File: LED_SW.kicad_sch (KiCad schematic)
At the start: 32 parts

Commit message: OLED, Relay and Bar graph added
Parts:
- renumbered D to D10, D to D11, D to D12, D to D13, D to D14, D to D15, D to D16, D to D9, R to R12, R to R13, R to R14, R to R15, R to R16, R to R17, R to R18, R to R19, S to S2, S to S3, S to S4, S to S5, S to S6, S to S7, S to S8, S to S9

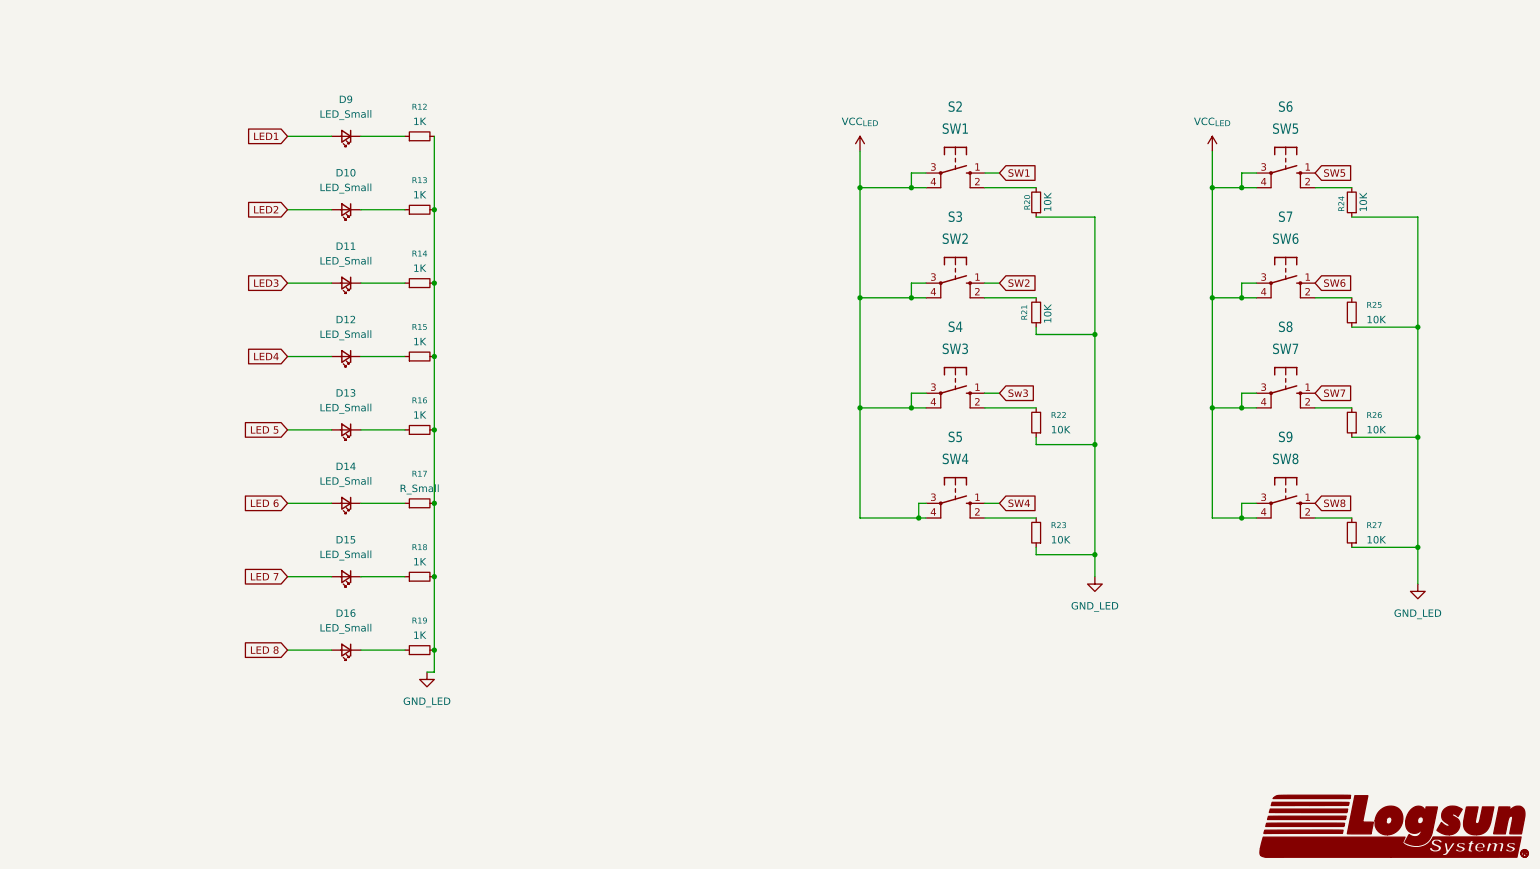
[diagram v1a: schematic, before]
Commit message: Connectors Added
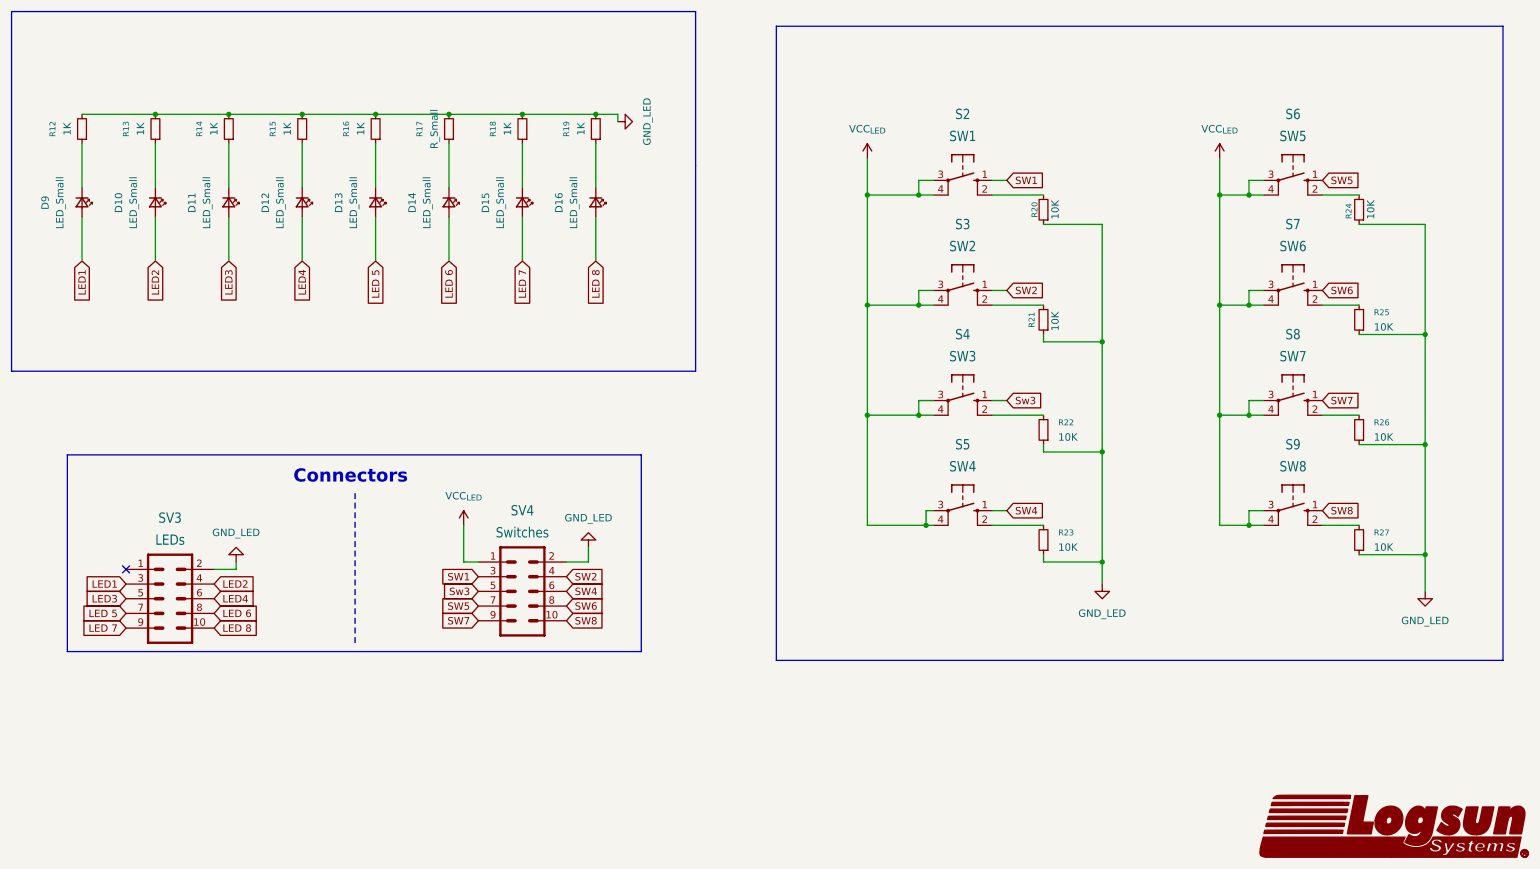
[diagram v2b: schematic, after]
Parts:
- added SV3: LEDs, LOGSUN:LGS-KC-ML10_INTERFACE, symbol LOGSUN:LGS-KC-ML10_INTERFACE
- added SV4: Switches, LOGSUN:LGS-KC-ML10_INTERFACE, symbol LOGSUN:LGS-KC-ML10_INTERFACE
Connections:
- net GND_LED: now also SV3.2, SV4.2
- net LED 5: now also SV3.7
- net LED 6: now also SV3.8
- net LED 7: now also SV3.9
- net LED 8: now also SV3.10
- net LED1: now also SV3.3
- net LED2: now also SV3.4
- net LED3: now also SV3.5
- net LED4: now also SV3.6
- net SW1: now also SV4.3
- net SW2: now also SV4.4
- net SW4: now also SV4.6
- net SW5: now also SV4.7
- net SW6: now also SV4.8
- net SW7: now also SV4.9
- net SW8: now also SV4.10
- net Sw3: now also SV4.5
- net VCC_{LED}: now also SV4.1
- no-connect marks 0 -> 1
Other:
- note added: "Connectors"
- moved on the sheet: D10, D11, D12, D13, D14, D15, D16, D9, R12, R13, R14, R15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

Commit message: Schematic Completed, Footprints Assigned
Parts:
- D10, D11, D12, D13, D14, D15, D16, D9: footprint (none) -> LED_SMD:LED_1206_3216Metric_ReverseMount_Hole1.8x2.4mm
- R12, R13, R14, R15, R16, R18, R19, R20, R21, R22, R23, R24, R25, R26, R27: footprint (none) -> Resistor_SMD:R_0805_2012Metric_Pad1.20x1.40mm_HandSolder
- R17: value R_Small -> 1K; footprint (none) -> Resistor_SMD:R_0805_2012Metric_Pad1.20x1.40mm_HandSolder
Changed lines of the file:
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@@
 			)
 		)
-		(property "Footprint" ""
+		(property "Footprint" "Resistor_SMD:R_0805_2012Metric_Pad1.20x1.40mm_HandSolder"
 			(at 105.41 53.34 0)
 			(effects
@@
 			)
 		)
-		(property "Footprint" ""
+		(property "Footprint" "LED_SMD:LED_1206_3216Metric_ReverseMount_Hole1.8x2.4mm"
 			(at 54.61 66.04 90)
 			(effects
@@
 			)
 		)
-		(property "Footprint" ""
+		(property "Footprint" "Resistor_SMD:R_0805_2012Metric_Pad1.20x1.40mm_HandSolder"
 			(at 80.01 53.34 0)
 			(effects
@@
 			)
 		)
-		(property "Footprint" ""
+		(property "Footprint" "Resistor_SMD:R_0805_2012Metric_Pad1.20x1.40mm_HandSolder"
 			(at 195.58 67.31 0)
 			(effects
@@
 		(fields_autoplaced yes)
 		(property "Reference" "R17"
-			(at 87.63 53.34 90)
+			(at 95.25 52.0699 0)
 			(effects
 				(font
 					(size 1.016 1.016)
 				)
-			)
-		)
-		(property "Value" "R_Small"
-			(at 90.17 53.34 90)
-			(effects
-				(font
-					(size 1.27 1.27)
-				)
-			)
-		)
-		(property "Footprint" ""
+				(justify right)
+			)
+		)
+		(property "Value" "1K"
+			(at 95.25 54.6099 0)
+			(effects
+				(font
+					(size 1.27 1.27)
+				)
+				(justify right)
+			)
+		)
+		(property "Footprint" "Resistor_SMD:R_0805_2012Metric_Pad1.20x1.40mm_HandSolder"
 			(at 92.71 53.34 0)
 			(effects
@@
 			)
 		)
-		(property "Footprint" ""
+		(property "Footprint" "LED_SMD:LED_1206_3216Metric_ReverseMount_Hole1.8x2.4mm"
 			(at 29.21 66.04 90)
 			(effects
@@
 			)
 		)
-		(property "Footprint" ""
+		(property "Footprint" "LED_SMD:LED_1206_3216Metric_ReverseMount_Hole1.8x2.4mm"
 			(at 92.71 66.04 90)
 			(effects
@@
 			)
 		)
-		(property "Footprint" ""
+		(property "Footprint" "Resistor_SMD:R_0805_2012Metric_Pad1.20x1.40mm_HandSolder"
 			(at 250.19 67.31 0)
 			(effects
@@
 			)
 		)
-		(property "Footprint" ""
+		(property "Footprint" "LED_SMD:LED_1206_3216Metric_ReverseMount_Hole1.8x2.4mm"
 			(at 118.11 66.04 90)
 			(effects
@@
 			)
 		)
-		(property "Footprint" ""
+		(property "Footprint" "Resistor_SMD:R_0805_2012Metric_Pad1.20x1.40mm_HandSolder"
 			(at 250.19 124.46 0)
 			(effects
@@
 			)
 		)
-		(property "Footprint" ""
+		(property "Footprint" "Resistor_SMD:R_0805_2012Metric_Pad1.20x1.40mm_HandSolder"
 			(at 41.91 53.34 0)
 			(effects
@@
 			)
 		)
-		(property "Footprint" ""
+		(property "Footprint" "LED_SMD:LED_1206_3216Metric_ReverseMount_Hole1.8x2.4mm"
 			(at 80.01 66.04 90)
 			(effects
@@
 			)
 		)
-		(property "Footprint" ""
+		(property "Footprint" "Resistor_SMD:R_0805_2012Metric_Pad1.20x1.40mm_HandSolder"
 			(at 29.21 53.34 0)
 			(effects
@@
 			)
 		)
-		(property "Footprint" ""
+		(property "Footprint" "Resistor_SMD:R_0805_2012Metric_Pad1.20x1.40mm_HandSolder"
 			(at 118.11 53.34 0)
 			(effects
@@
 			)
 		)
-		(property "Footprint" ""
+		(property "Footprint" "LED_SMD:LED_1206_3216Metric_ReverseMount_Hole1.8x2.4mm"
 			(at 67.31 66.04 90)
 			(effects
@@
 			)
 		)
-		(property "Footprint" ""
+		(property "Footprint" "Resistor_SMD:R_0805_2012Metric_Pad1.20x1.40mm_HandSolder"
 			(at 250.19 86.36 0)
 			(effects
@@
 			)
 		)
-		(property "Footprint" ""
+		(property "Footprint" "LED_SMD:LED_1206_3216Metric_ReverseMount_Hole1.8x2.4mm"
 			(at 105.41 66.04 90)
 			(effects
@@
 			)
 		)
-		(property "Footprint" ""
+		(property "Footprint" "LED_SMD:LED_1206_3216Metric_ReverseMount_Hole1.8x2.4mm"
 			(at 41.91 66.04 90)
 			(effects
@@
 			)
 		)
-		(property "Footprint" ""
+		(property "Footprint" "Resistor_SMD:R_0805_2012Metric_Pad1.20x1.40mm_HandSolder"
 			(at 54.61 53.34 0)
 			(effects
@@
 			)
 		)
-		(property "Footprint" ""
+		(property "Footprint" "Resistor_SMD:R_0805_2012Metric_Pad1.20x1.40mm_HandSolder"
 			(at 195.58 105.41 0)
 			(effects
@@
 			)
 		)
-		(property "Footprint" ""
+		(property "Footprint" "Resistor_SMD:R_0805_2012Metric_Pad1.20x1.40mm_HandSolder"
 			(at 250.19 105.41 0)
 			(effects
@@
 			)
 		)
-		(property "Footprint" ""
+		(property "Footprint" "Resistor_SMD:R_0805_2012Metric_Pad1.20x1.40mm_HandSolder"
 			(at 67.31 53.34 0)
 			(effects
@@
 			)
 		)
-		(property "Footprint" ""
+		(property "Footprint" "Resistor_SMD:R_0805_2012Metric_Pad1.20x1.40mm_HandSolder"
 			(at 195.58 124.46 0)
 			(effects
@@
 			)
 		)
-		(property "Footprint" ""
+		(property "Footprint" "Resistor_SMD:R_0805_2012Metric_Pad1.20x1.40mm_HandSolder"
 			(at 195.58 86.36 0)
 			(effects

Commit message: Bar LED Resistors Added & Mounting holes added
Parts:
- D10, D11, D12, D13, D14, D15, D16, D9: footprint LED_SMD:LED_1206_3216Metric_ReverseMount_Hole1.8x2.4mm -> LED_SMD:LED_1206_3216Metric_Pad1.42x1.75mm_HandSolder
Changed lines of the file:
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@@
 			)
 		)
-		(property "Footprint" "LED_SMD:LED_1206_3216Metric_ReverseMount_Hole1.8x2.4mm"
+		(property "Footprint" "LED_SMD:LED_1206_3216Metric_Pad1.42x1.75mm_HandSolder"
 			(at 54.61 66.04 90)
 			(effects
@@
 			)
 		)
-		(property "Footprint" "LED_SMD:LED_1206_3216Metric_ReverseMount_Hole1.8x2.4mm"
+		(property "Footprint" "LED_SMD:LED_1206_3216Metric_Pad1.42x1.75mm_HandSolder"
 			(at 29.21 66.04 90)
 			(effects
@@
 			)
 		)
-		(property "Footprint" "LED_SMD:LED_1206_3216Metric_ReverseMount_Hole1.8x2.4mm"
+		(property "Footprint" "LED_SMD:LED_1206_3216Metric_Pad1.42x1.75mm_HandSolder"
 			(at 92.71 66.04 90)
 			(effects
@@
 			)
 		)
-		(property "Footprint" "LED_SMD:LED_1206_3216Metric_ReverseMount_Hole1.8x2.4mm"
+		(property "Footprint" "LED_SMD:LED_1206_3216Metric_Pad1.42x1.75mm_HandSolder"
 			(at 118.11 66.04 90)
 			(effects
@@
 			)
 		)
-		(property "Footprint" "LED_SMD:LED_1206_3216Metric_ReverseMount_Hole1.8x2.4mm"
+		(property "Footprint" "LED_SMD:LED_1206_3216Metric_Pad1.42x1.75mm_HandSolder"
 			(at 80.01 66.04 90)
 			(effects
@@
 			)
 		)
-		(property "Footprint" "LED_SMD:LED_1206_3216Metric_ReverseMount_Hole1.8x2.4mm"
+		(property "Footprint" "LED_SMD:LED_1206_3216Metric_Pad1.42x1.75mm_HandSolder"
 			(at 67.31 66.04 90)
 			(effects
@@
 			)
 		)
-		(property "Footprint" "LED_SMD:LED_1206_3216Metric_ReverseMount_Hole1.8x2.4mm"
+		(property "Footprint" "LED_SMD:LED_1206_3216Metric_Pad1.42x1.75mm_HandSolder"
 			(at 105.41 66.04 90)
 			(effects
@@
 			)
 		)
-		(property "Footprint" "LED_SMD:LED_1206_3216Metric_ReverseMount_Hole1.8x2.4mm"
+		(property "Footprint" "LED_SMD:LED_1206_3216Metric_Pad1.42x1.75mm_HandSolder"
 			(at 41.91 66.04 90)
 			(effects

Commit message: Symbol and footprint library exported
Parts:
- D10, D11, D12, D13, D14, D15, D16, D9: symbol Device:LED_Small -> ESP32_Xbee_LoRa:LED_Small
- R12, R13, R14, R15, R16, R17, R18, R19, R20, R21, R22, R23, R24, R25, R26, R27: symbol Device:R_Small -> ESP32_Xbee_LoRa:R_Small
- S2, S3, S4, S5, S6, S7, S8, S9: symbol LOGSUN:LGS-KC-10-XX -> ESP32_Xbee_LoRa:LGS-KC-10-XX
- SV3, SV4: symbol LOGSUN:LGS-KC-ML10_INTERFACE -> ESP32_Xbee_LoRa:LGS-KC-ML10_INTERFACE
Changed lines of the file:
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@@
 	)
 	(symbol
-		(lib_id "power:VCC")
+		(lib_id "ESP32_Xbee_LoRa:VCC")
 		(at 165.1 58.42 0)
 		(unit 1)
@@
 	)
 	(symbol
-		(lib_id "LOGSUN:LGS-KC-10-XX")
+		(lib_id "ESP32_Xbee_LoRa:LGS-KC-10-XX")
 		(at 238.76 119.38 270)
 		(unit 1)
@@
 	)
 	(symbol
-		(lib_id "Device:R_Small")
+		(lib_id "ESP32_Xbee_LoRa:R_Small")
 		(at 105.41 53.34 180)
 		(unit 1)
@@
 	)
 	(symbol
-		(lib_id "LOGSUN:LGS-KC-ML10_INTERFACE")
+		(lib_id "ESP32_Xbee_LoRa:LGS-KC-ML10_INTERFACE")
 		(at 44.45 134.62 180)
 		(unit 1)
@@
 	)
 	(symbol
-		(lib_id "Device:LED_Small")
+		(lib_id "ESP32_Xbee_LoRa:LED_Small")
 		(at 54.61 66.04 270)
 		(unit 1)
@@
 	)
 	(symbol
-		(lib_id "power:GND")
+		(lib_id "ESP32_Xbee_LoRa:GND")
 		(at 205.74 132.08 0)
 		(unit 1)
@@
 	)
 	(symbol
-		(lib_id "Device:R_Small")
+		(lib_id "ESP32_Xbee_LoRa:R_Small")
 		(at 80.01 53.34 180)
 		(unit 1)
@@
 	)
 	(symbol
-		(lib_id "Device:R_Small")
+		(lib_id "ESP32_Xbee_LoRa:R_Small")
 		(at 195.58 67.31 180)
 		(unit 1)
@@
 	)
 	(symbol
-		(lib_id "Device:R_Small")
+		(lib_id "ESP32_Xbee_LoRa:R_Small")
 		(at 92.71 53.34 180)
 		(unit 1)
@@
 	)
 	(symbol
-		(lib_id "Device:LED_Small")
+		(lib_id "ESP32_Xbee_LoRa:LED_Small")
 		(at 29.21 66.04 270)
 		(unit 1)
@@
 	)
 	(symbol
-		(lib_id "LOGSUN:LGS-KC-ML10_INTERFACE")
+		(lib_id "ESP32_Xbee_LoRa:LGS-KC-ML10_INTERFACE")
 		(at 105.41 133.35 180)
 		(unit 1)
@@
 	)
 	(symbol
-		(lib_id "LOGSUN:LGS-KC-10-XX")
+		(lib_id "ESP32_Xbee_LoRa:LGS-KC-10-XX")
 		(at 238.76 62.23 270)
 		(unit 1)
@@
 	)
 	(symbol
-		(lib_id "power:VCC")
+		(lib_id "ESP32_Xbee_LoRa:VCC")
 		(at 95.25 121.92 0)
 		(unit 1)
@@
 	)
 	(symbol
-		(lib_id "Device:LED_Small")
+		(lib_id "ESP32_Xbee_LoRa:LED_Small")
 		(at 92.71 66.04 270)
 		(unit 1)
@@
 	)
 	(symbol
-		(lib_id "power:GND")
+		(lib_id "ESP32_Xbee_LoRa:GND")
 		(at 121.92 52.07 90)
 		(unit 1)
@@
 	)
 	(symbol
-		(lib_id "Device:R_Small")
+		(lib_id "ESP32_Xbee_LoRa:R_Small")
 		(at 250.19 67.31 180)
 		(unit 1)
@@
 	)
 	(symbol
-		(lib_id "Device:LED_Small")
+		(lib_id "ESP32_Xbee_LoRa:LED_Small")
 		(at 118.11 66.04 270)
 		(unit 1)
@@
 	)
 	(symbol
-		(lib_id "Device:R_Small")
+		(lib_id "ESP32_Xbee_LoRa:R_Small")
 		(at 250.19 124.46 180)
 		(unit 1)
@@
 	)
 	(symbol
-		(lib_id "Device:R_Small")
+		(lib_id "ESP32_Xbee_LoRa:R_Small")
 		(at 41.91 53.34 180)
 		(unit 1)
@@
 	)
 	(symbol
-		(lib_id "Device:LED_Small")
+		(lib_id "ESP32_Xbee_LoRa:LED_Small")
 		(at 80.01 66.04 270)
 		(unit 1)
@@
 	)
 	(symbol
-		(lib_id "power:GND")
+		(lib_id "ESP32_Xbee_LoRa:GND")
 		(at 261.62 133.35 0)
 		(unit 1)
@@
 	)
 	(symbol
-		(lib_id "Device:R_Small")
+		(lib_id "ESP32_Xbee_LoRa:R_Small")
 		(at 29.21 53.34 180)
 		(unit 1)
@@
 	)
 	(symbol
-		(lib_id "Device:R_Small")
+		(lib_id "ESP32_Xbee_LoRa:R_Small")
 		(at 118.11 53.34 180)
 		(unit 1)
@@
 	)
 	(symbol
-		(lib_id "LOGSUN:LGS-KC-10-XX")
+		(lib_id "ESP32_Xbee_LoRa:LGS-KC-10-XX")
 		(at 238.76 81.28 270)
 		(unit 1)
@@
 	)
 	(symbol
-		(lib_id "Device:LED_Small")
+		(lib_id "ESP32_Xbee_LoRa:LED_Small")
 		(at 67.31 66.04 270)
 		(unit 1)
@@
 	)
 	(symbol
-		(lib_id "power:GND")
+		(lib_id "ESP32_Xbee_LoRa:GND")
 		(at 116.84 125.73 180)
 		(unit 1)
@@
 	)
 	(symbol
-		(lib_id "Device:R_Small")
+		(lib_id "ESP32_Xbee_LoRa:R_Small")
 		(at 250.19 86.36 180)
 		(unit 1)
@@
 	)
 	(symbol
-		(lib_id "Device:LED_Small")
+		(lib_id "ESP32_Xbee_LoRa:LED_Small")
 		(at 105.41 66.04 270)
 		(unit 1)
@@
 	)
 	(symbol
-		(lib_id "Device:LED_Small")
+		(lib_id "ESP32_Xbee_LoRa:LED_Small")
 		(at 41.91 66.04 270)
 		(unit 1)
@@
 	)
 	(symbol
-		(lib_id "power:VCC")
+		(lib_id "ESP32_Xbee_LoRa:VCC")
 		(at 226.06 58.42 0)
 		(unit 1)
@@
 	)
 	(symbol
-		(lib_id "LOGSUN:LGS-KC-10-XX")
+		(lib_id "ESP32_Xbee_LoRa:LGS-KC-10-XX")
 		(at 181.61 119.38 270)
 		(unit 1)
@@
 	)
 	(symbol
-		(lib_id "LOGSUN:LGS-KC-10-XX")
+		(lib_id "ESP32_Xbee_LoRa:LGS-KC-10-XX")
 		(at 238.76 100.33 270)
 		(unit 1)
@@
 	)
 	(symbol
-		(lib_id "LOGSUN:LGS-KC-10-XX")
+		(lib_id "ESP32_Xbee_LoRa:LGS-KC-10-XX")
 		(at 181.61 100.33 270)
 		(unit 1)
@@
 	)
 	(symbol
-		(lib_id "Device:R_Small")
+		(lib_id "ESP32_Xbee_LoRa:R_Small")
 		(at 54.61 53.34 180)
 		(unit 1)
@@
 	)
 	(symbol
-		(lib_id "Device:R_Small")
+		(lib_id "ESP32_Xbee_LoRa:R_Small")
 		(at 195.58 105.41 180)
 		(unit 1)
@@
 	)
 	(symbol
-		(lib_id "LOGSUN:LGS-KC-10-XX")
+		(lib_id "ESP32_Xbee_LoRa:LGS-KC-10-XX")
 		(at 181.61 81.28 270)
 		(unit 1)
@@
 	)
 	(symbol
-		(lib_id "LOGSUN:LGS-KC-10-XX")
+		(lib_id "ESP32_Xbee_LoRa:LGS-KC-10-XX")
 		(at 181.61 62.23 270)
 		(unit 1)
@@
 	)
 	(symbol
-		(lib_id "Device:R_Small")
+		(lib_id "ESP32_Xbee_LoRa:R_Small")
 		(at 250.19 105.41 180)
 		(unit 1)
@@
 	)
 	(symbol
-		(lib_id "power:GND")
+		(lib_id "ESP32_Xbee_LoRa:GND")
 		(at 55.88 128.27 180)
 		(unit 1)
@@
 	)
 	(symbol
-		(lib_id "Logsun_Logo:LOGO")
+		(lib_id "ESP32_Xbee_LoRa:LOGO")
 		(at 256.54 173.99 0)
 		(unit 1)
@@
 	)
 	(symbol
-		(lib_id "Device:R_Small")
+		(lib_id "ESP32_Xbee_LoRa:R_Small")
 		(at 67.31 53.34 180)
 		(unit 1)
@@
 	)
 	(symbol
-		(lib_id "Device:R_Small")
+		(lib_id "ESP32_Xbee_LoRa:R_Small")
 		(at 195.58 124.46 180)
 		(unit 1)
@@
 	)
 	(symbol
-		(lib_id "Device:R_Small")
+		(lib_id "ESP32_Xbee_LoRa:R_Small")
 		(at 195.58 86.36 180)
 		(unit 1)
